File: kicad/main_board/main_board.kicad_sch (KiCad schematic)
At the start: 8 parts

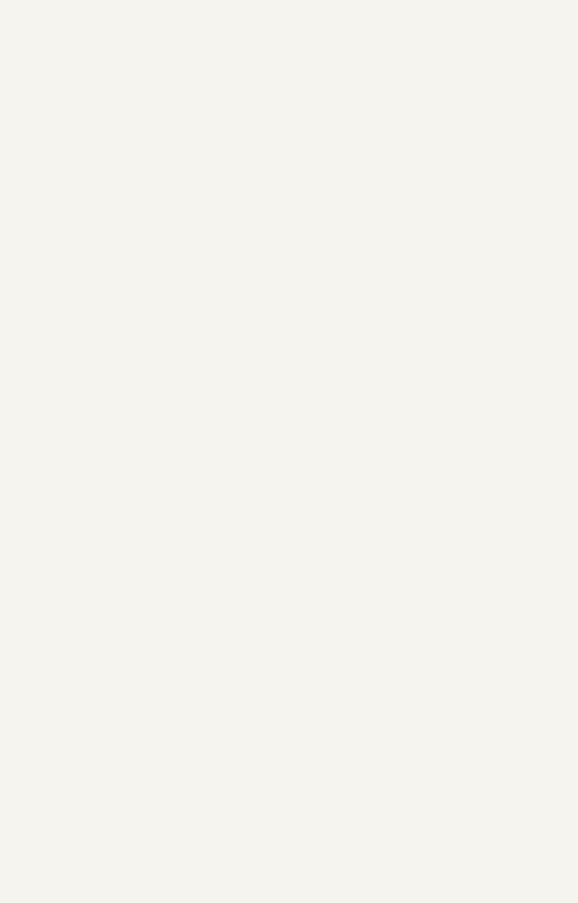
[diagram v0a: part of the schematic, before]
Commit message: add controller
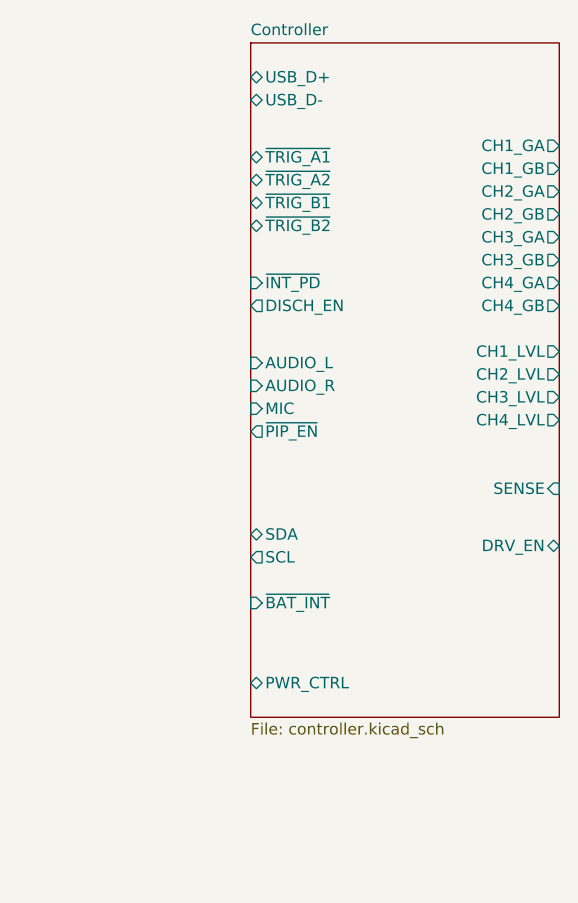
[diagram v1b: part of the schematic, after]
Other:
- added sheet Controller (controller.kicad_sch)

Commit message: add output
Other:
- added sheet Output (output.kicad_sch)
- note added: "MCU"
- note added: "Output Board Connections"

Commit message: add power
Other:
- added sheet Power (power.kicad_sch)
- note added: "PSUs, Soft Power Switch"
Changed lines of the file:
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@@
+	(wire
+		(pts
+			(xy 149.86 123.19) (xy 172.72 123.19)
+		)
+		(stroke
+			(width 0)
+			(type default)
+		)
+	)
 	(wire
 		(pts
@@
 	(text "Output Board Connections"
 		(exclude_from_sim no)
-		(at 232.156 107.696 0)
+		(at 232.156 107.95 0)
 		(effects
 			(font
@@
 	(text "MCU"
 		(exclude_from_sim no)
-		(at 188.468 131.064 0)
+		(at 188.468 130.81 0)
+		(effects
+			(font
+				(size 1 1)
+			)
+			(justify top)
+		)
+	)
+	(text "PSUs, Soft Power Switch"
+		(exclude_from_sim no)
+		(at 136.652 130.81 0)
 		(effects
 			(font
@@
 	)
 	(sheet
+		(at 123.19 119.38)
+		(size 26.67 7.62)
+		(fields_autoplaced yes)
+		(stroke
+			(width 0.1524)
+			(type solid)
+		)
+		(fill
+			(color 0 0 0 0.0000)
+		)
+		(property "Sheetname" "Power"
+			(at 123.19 118.6684 0)
+			(effects
+				(font
+					(size 1.27 1.27)
+				)
+				(justify left bottom)
+			)
+		)
+		(property "Sheetfile" "power.kicad_sch"
+			(at 123.19 127.5846 0)
+			(effects
+				(font
+					(size 1.27 1.27)
+				)
+				(justify left top)
+			)
+		)
+		(pin "~{WAKE}" output
+			(at 123.19 123.19 180)
+			(effects
+				(font
+					(size 1.27 1.27)
+				)
+				(justify left)
+			)
+		)
+		(pin "PWR_CTRL" bidirectional
+			(at 149.86 123.19 0)
+			(effects
+				(font
+					(size 1.27 1.27)
+				)
+				(justify right)
+			)
+		)
+		(instances
+			(project "main_board"
+				(path "/8e1f1504-76c2-49e6-9261-3c1190503f8c"
+					(page "4")
+				)
+			)
+		)
+	)
+	(sheet
 		(at 172.72 44.45)
 		(size 34.29 82.55)
@@
 		)
 		(pin "~{BAT_INT}" input
-			(at 172.72 115.57 180)
+			(at 172.72 111.76 180)
 			(effects
 				(font
@@
 		)
 		(pin "SDA" bidirectional
-			(at 172.72 109.22 180)
+			(at 172.72 105.41 180)
 			(effects
 				(font
@@
 		)
 		(pin "SCL" output
-			(at 172.72 111.76 180)
+			(at 172.72 107.95 180)
 			(effects
 				(font
@@
 		)
 		(pin "PWR_CTRL" bidirectional
-			(at 172.72 124.46 180)
-			(effects
-				(font
+			(at 172.72 123.19 180)
+			(effects
+				(font

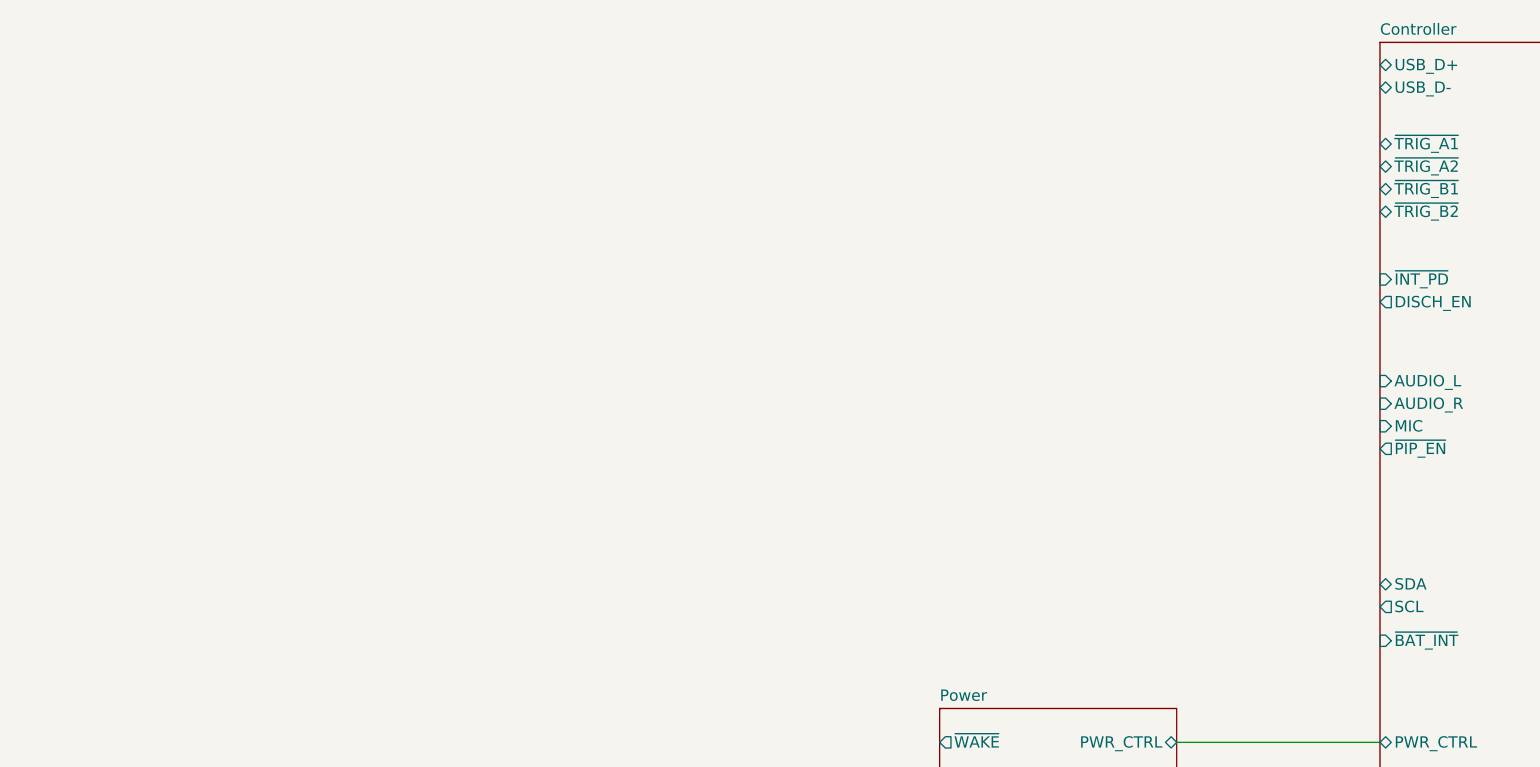
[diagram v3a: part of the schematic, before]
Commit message: add input
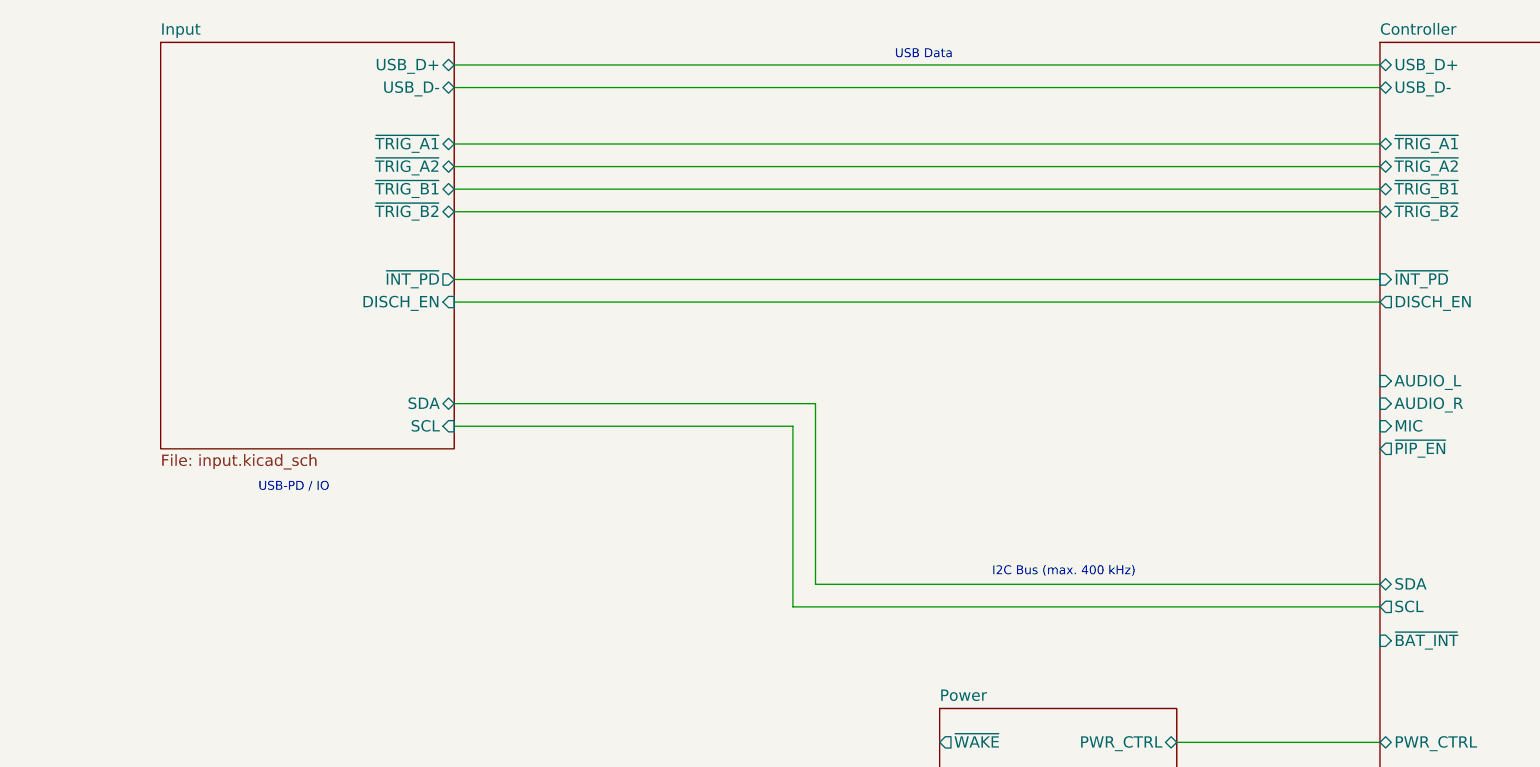
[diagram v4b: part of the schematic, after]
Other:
- added sheet Input (input.kicad_sch)
- note added: "I2C Bus (max. 400 kHz)"
- note added: "USB Data"
- note added: "USB-PD / IO"

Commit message: add audio
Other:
- added sheet Audio (audio.kicad_sch)
- note added: "Analog Audio"
- note added: "Line/Mic Level Audio -> 0-3.3V MCU Controlled Gain"
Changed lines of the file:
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@@
 		(company "saawsm")
 	)
+	(junction
+		(at 106.68 87.63)
+		(diameter 0)
+		(color 0 0 0 0)
+	)
+	(junction
+		(at 109.22 85.09)
+		(diameter 0)
+		(color 0 0 0 0)
+	)
 	(wire
 		(pts
@@
 	(wire
 		(pts
+			(xy 106.68 87.63) (xy 124.46 87.63)
+		)
+		(stroke
+			(width 0)
+			(type default)
+		)
+	)
+	(wire
+		(pts
+			(xy 151.13 90.17) (xy 172.72 90.17)
+		)
+		(stroke
+			(width 0)
+			(type default)
+		)
+	)
+	(wire
+		(pts
 			(xy 207.01 59.69) (xy 217.17 59.69)
 		)
@@
 	(wire
 		(pts
+			(xy 151.13 82.55) (xy 172.72 82.55)
+		)
+		(stroke
+			(width 0)
+			(type default)
+		)
+	)
+	(wire
+		(pts
+			(xy 151.13 87.63) (xy 172.72 87.63)
+		)
+		(stroke
+			(width 0)
+			(type default)
+		)
+	)
+	(wire
+		(pts
 			(xy 149.86 123.19) (xy 172.72 123.19)
 		)
@@
 	(wire
 		(pts
+			(xy 109.22 85.09) (xy 124.46 85.09)
+		)
+		(stroke
+			(width 0)
+			(type default)
+		)
+	)
+	(wire
+		(pts
 			(xy 68.58 87.63) (xy 106.68 87.63)
+		)
+		(stroke
+			(width 0)
+			(type default)
+		)
+	)
+	(wire
+		(pts
+			(xy 151.13 85.09) (xy 172.72 85.09)
 		)
 		(stroke
@@
 			)
 			(justify top)
+		)
+	)
+	(text "Line/Mic Level Audio -> 0-3.3V \nMCU Controlled Gain"
+		(exclude_from_sim no)
+		(at 125.222 98.806 0)
+		(effects
+			(font
+				(size 1 1)
+			)
+			(justify left bottom)
+		)
+	)
+	(text "Analog Audio"
+		(exclude_from_sim no)
+		(at 157.734 81.788 0)
+		(effects
+			(font
+				(size 1 1)
+			)
+			(justify left bottom)
 		)
 	)
@@
 				)
 			)
+		)
+	)
+	(sheet
+		(at 124.46 80.01)
+		(size 26.67 12.7)
+		(fields_autoplaced yes)
+		(stroke
+			(width 0.1524)
+			(type solid)
+		)
+		(fill
+			(color 0 0 0 0.0000)
+		)
+		(property "Sheetname" "Audio"
+			(at 124.46 79.2984 0)
+			(effects
+				(font
+					(size 1.27 1.27)
+				)
+				(justify left bottom)
+			)
+		)
+		(property "Sheetfile" "audio.kicad_sch"
+			(at 124.46 93.2946 0)
+			(effects
+				(font
+					(size 1.27 1.27)
+				)
+				(justify left top)
+			)
+		)
+		(pin "SCL" input
+			(at 124.46 87.63 180)
+			(effects
+				(font
+					(size 1.27 1.27)
+				)
+				(justify left)
+			)
+		)
+		(pin "SDA" bidirectional
+			(at 124.46 85.09 180)
+			(effects
+				(font
+					(size 1.27 1.27)
+				)
+				(justify left)
+			)
+		)
+		(pin "~{PIP_EN}" input
+			(at 151.13 90.17 0)
+			(effects
+				(font
+					(size 1.27 1.27)
+				)
+				(justify right)
+			)
+		)
+		(pin "MIC" output
+			(at 151.13 87.63 0)
+			(effects
+				(font
+					(size 1.27 1.27)
+				)
+				(justify right)
+			)
+		)
+		(pin "AUDIO_L" output
+			(at 151.13 82.55 0)
+			(effects
+				(font
+					(size 1.27 1.27)
+				)
+				(justify right)
+			)
+		)
+		(pin "AUDIO_R" output
+			(at 151.13 85.09 0)
+			(effects
+				(font
+					(size 1.27 1.27)
+				)
+				(justify right)
+			)
+		)
+		(instances
+			(project "main_board"
+				(path "/8e1f1504-76c2-49e6-9261-3c1190503f8c"
+					(page "6")
+				)
+			)

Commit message: add charger
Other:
- added sheet Charger (charger.kicad_sch)
- note added: "Battery Charger"

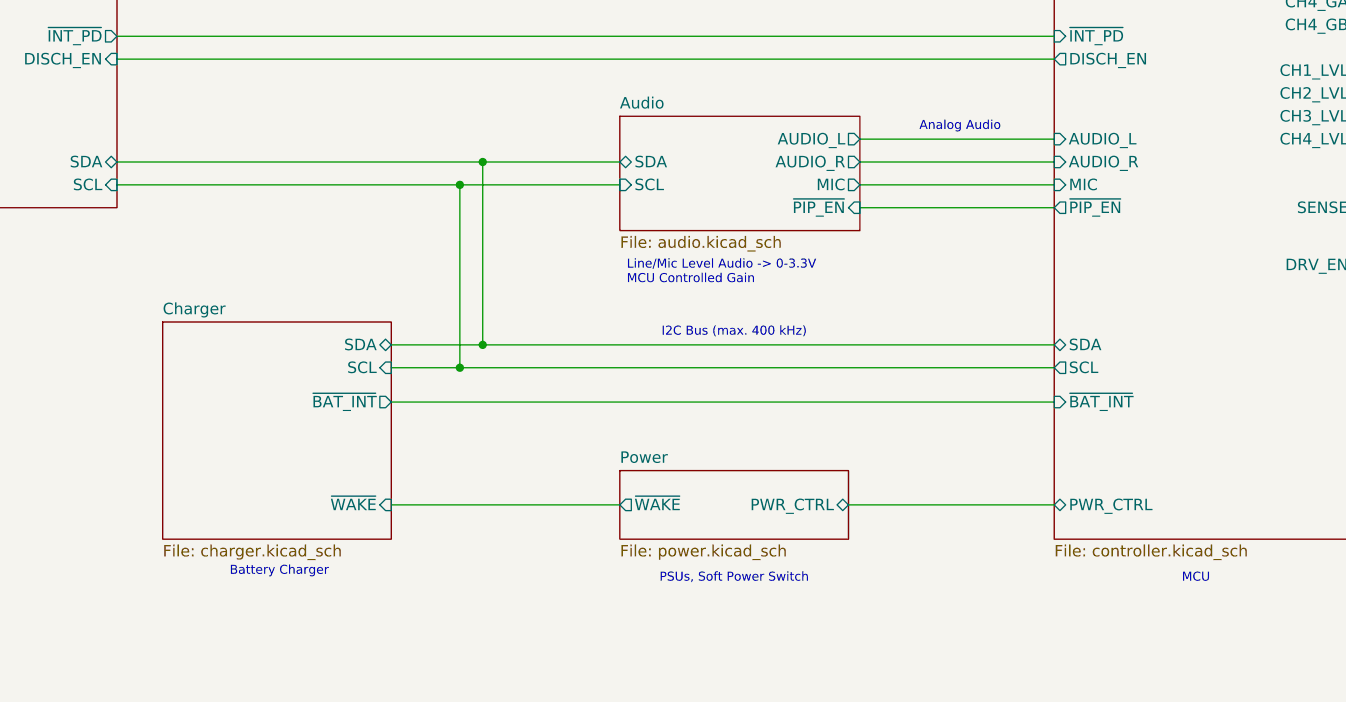
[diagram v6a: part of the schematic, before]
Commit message: add I2S link
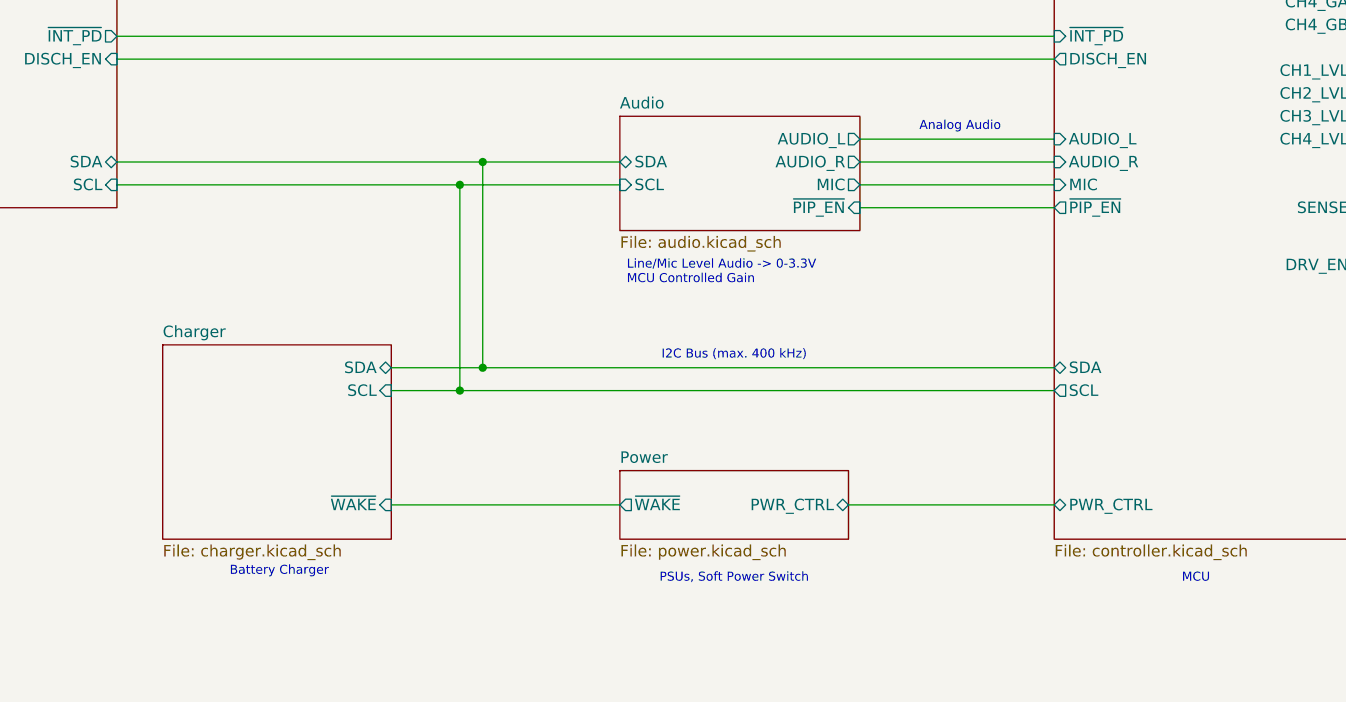
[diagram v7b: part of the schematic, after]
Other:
- sheet Charger ports: added none; removed ~{BAT_INT}
- sheet Controller ports: added none; removed ~{BAT_INT}
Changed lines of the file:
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@@
 	(title_block
 		(title "SW32 - Main Board")
-		(date "2024-05-22")
+		(date "2024-05-23")
 		(rev "1")
 		(company "saawsm")
@@
 	)
 	(junction
-		(at 114.3 105.41)
+		(at 114.3 107.95)
 		(diameter 0)
 		(color 0 0 0 0)
 	)
 	(junction
-		(at 111.76 107.95)
+		(at 111.76 110.49)
 		(diameter 0)
 		(color 0 0 0 0)
@@
 	(wire
 		(pts
-			(xy 111.76 107.95) (xy 177.8 107.95)
+			(xy 111.76 110.49) (xy 177.8 110.49)
 		)
 		(stroke
@@
 	(wire
 		(pts
-			(xy 114.3 85.09) (xy 114.3 105.41)
-		)
-		(stroke
-			(width 0)
-			(type default)
-		)
-	)
-	(wire
-		(pts
-			(xy 111.76 87.63) (xy 111.76 107.95)
+			(xy 114.3 85.09) (xy 114.3 107.95)
+		)
+		(stroke
+			(width 0)
+			(type default)
+		)
+	)
+	(wire
+		(pts
+			(xy 111.76 87.63) (xy 111.76 110.49)
 		)
 		(stroke
@@
 	(wire
 		(pts
-			(xy 114.3 105.41) (xy 177.8 105.41)
+			(xy 114.3 107.95) (xy 177.8 107.95)
 		)
 		(stroke
@@
 	(wire
 		(pts
-			(xy 104.14 111.76) (xy 177.8 111.76)
-		)
-		(stroke
-			(width 0)
-			(type default)
-		)
-	)
-	(wire
-		(pts
 			(xy 156.21 82.55) (xy 177.8 82.55)
 		)
@@
 	(wire
 		(pts
-			(xy 104.14 105.41) (xy 114.3 105.41)
+			(xy 104.14 107.95) (xy 114.3 107.95)
 		)
 		(stroke
@@
 	(wire
 		(pts
-			(xy 104.14 107.95) (xy 111.76 107.95)
+			(xy 104.14 110.49) (xy 111.76 110.49)
 		)
 		(stroke
@@
 	(text "I2C Bus (max. 400 kHz)"
 		(exclude_from_sim no)
-		(at 142.24 104.648 0)
+		(at 142.24 107.188 0)
 		(effects
 			(font
@@
 	)
 	(sheet
-		(at 78.74 102.87)
-		(size 25.4 24.13)
+		(at 78.74 105.41)
+		(size 25.4 21.59)
 		(fields_autoplaced yes)
 		(stroke
@@
 		)
 		(property "Sheetname" "Charger"
-			(at 78.74 102.1584 0)
+			(at 78.74 104.6984 0)
 			(effects
 				(font
@@
 		)
 		(pin "SCL" input
+			(at 104.14 110.49 0)
+			(effects
+				(font
+					(size 1.27 1.27)
+				)
+				(justify right)
+			)
+		)
+		(pin "SDA" bidirectional
 			(at 104.14 107.95 0)
-			(effects
-				(font
-					(size 1.27 1.27)
-				)
-				(justify right)
-			)
-		)
-		(pin "SDA" bidirectional
-			(at 104.14 105.41 0)
 			(effects
 				(font
@@
 		(pin "~{WAKE}" input
 			(at 104.14 123.19 0)
-			(effects
-				(font
-					(size 1.27 1.27)
-				)
-				(justify right)
-			)
-		)
-		(pin "~{BAT_INT}" output
-			(at 104.14 111.76 0)
 			(effects
 				(font
@@
 			)
 		)
-		(pin "~{BAT_INT}" input
-			(at 177.8 111.76 180)
-			(effects
-				(font
-					(size 1.27 1.27)
-				)
-				(justify left)
-			)
-		)
 		(pin "DRV_EN" bidirectional
 			(at 212.09 96.52 0)
@@
 		)
 		(pin "SDA" bidirectional
-			(at 177.8 105.41 180)
+			(at 177.8 107.95 180)
 			(effects
 				(font
@@
 		)
 		(pin "SCL" output
-			(at 177.8 107.95 180)
-			(effects
-				(font
+			(at 177.8 110.49 180)
+			(effects
+				(font
